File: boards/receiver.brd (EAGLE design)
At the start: 30 x 54.9 mm, 81 parts, among them IC2 7805DT, Q1 BC846BSMD, Q2 BC846BSMD, Q3 BC846BSMD, Q4 BC846BSMD, Q5 BC846BSMD, Q6 BC846BSMD, Q7 BC846BSMD, Q8 BC846BSMD

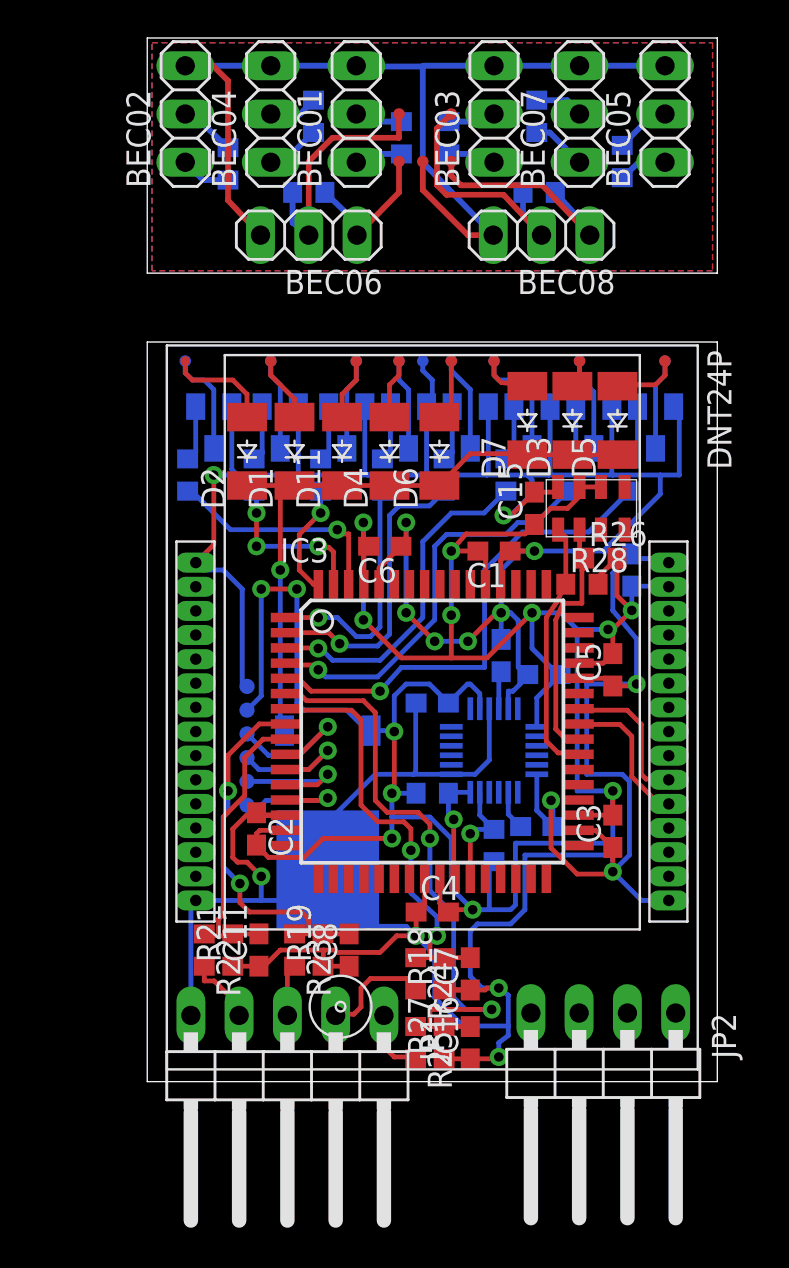
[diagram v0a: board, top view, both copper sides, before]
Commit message: Layout changes, all connections are routed now
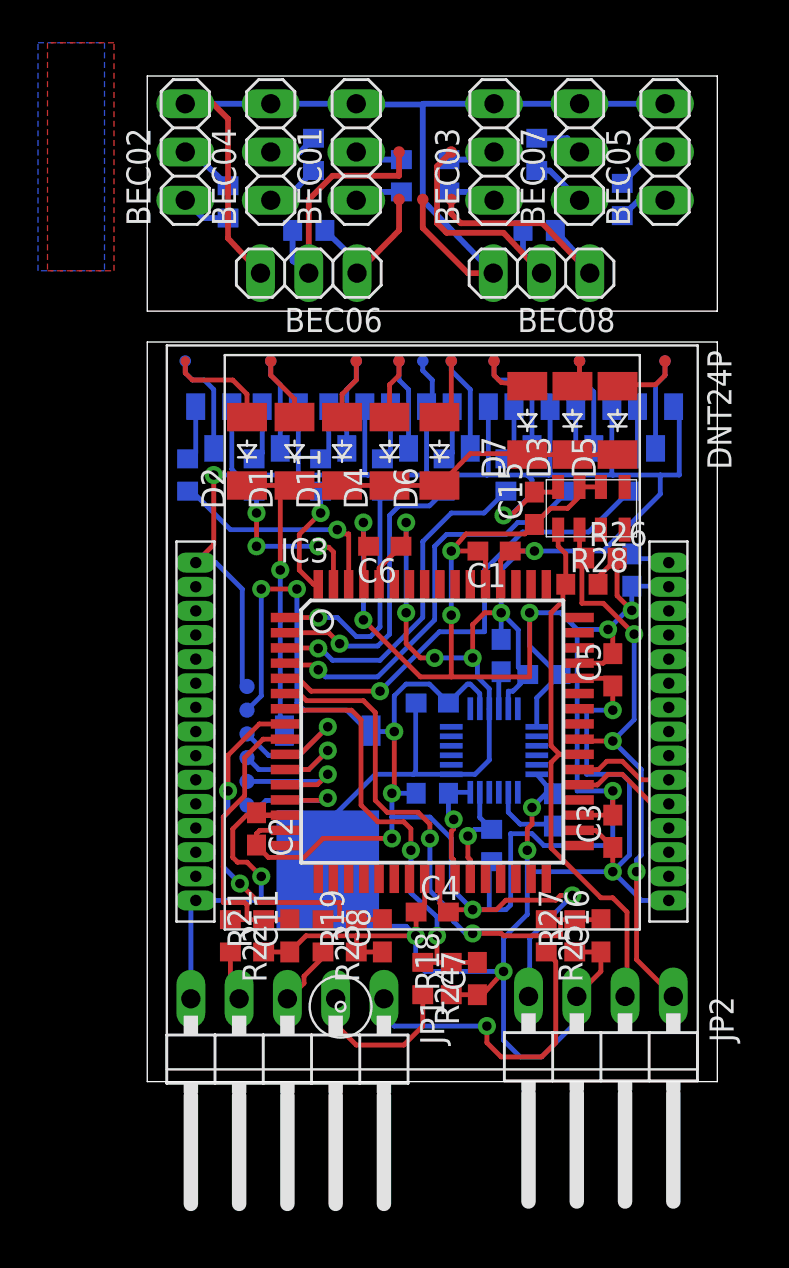
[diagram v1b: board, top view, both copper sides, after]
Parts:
- moved C16 8.88 mm to (24.9, 8.75)
- moved R25 8.88 mm to (22.0, 8.75)
- moved R27 8.88 mm to (23.5, 8.75)
- moved BEC01 2.00 mm to (12.0, 50.0)
- moved BEC02 2.00 mm to (3.00, 50.0)
- moved BEC03 2.00 mm to (19.2, 50.0)
- moved BEC04 2.00 mm to (7.50, 50.0)
- moved BEC05 2.00 mm to (28.2, 50.0)
- moved BEC06 2.00 mm to (9.50, 43.6)
- moved BEC07 2.00 mm to (23.8, 50.0)
- moved BEC08 2.00 mm to (21.8, 43.6)
- moved R10 2.00 mm to (26.0, 47.5)
- moved R12 2.00 mm to (9.50, 45.9)
- moved R14 2.00 mm to (21.5, 49.9)
- moved R16 2.00 mm to (21.6, 45.9)
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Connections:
- net +3V3: now also JP2.4
- net GND: now also JP2.3
- net N$33: now also IC3.37; no longer IC3.41
- net N$36: now also IC3.38; no longer IC3.42
- net N$46: now also JP2.2
- net N$47: now also JP2.1
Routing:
- net N$47: track 13.7 -> 30.7 mm, vias 0 -> 3
- net +3V3: track 149.3 -> 165.5 mm, vias 14 -> 15
- net N$46: track 13.6 -> 29.3 mm
- net GND: track 323.0 -> 308.9 mm
- net N$50: track 3.58 -> 16.6 mm, vias 0 -> 1
- net PB0: track 32.1 -> 28.5 mm
- net N$36: track 7.77 -> 5.28 mm
- net N$33: track 7.68 -> 5.58 mm
- net N$35: track 2.23 -> 4.24 mm
- net N$42: track 6.55 -> 8.45 mm
- net PB3: track 15.4 -> 16.9 mm
- net N$27: track 25.8 -> 24.7 mm
- net PB2: track 19.5 -> 20.6 mm
- net N$44: track 3.66 -> 2.66 mm
- net N$43: track 2.75 -> 3.61 mm
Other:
- board size 30 x 54.9 mm -> 30 x 52.9 mm

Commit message: rerouted some wires
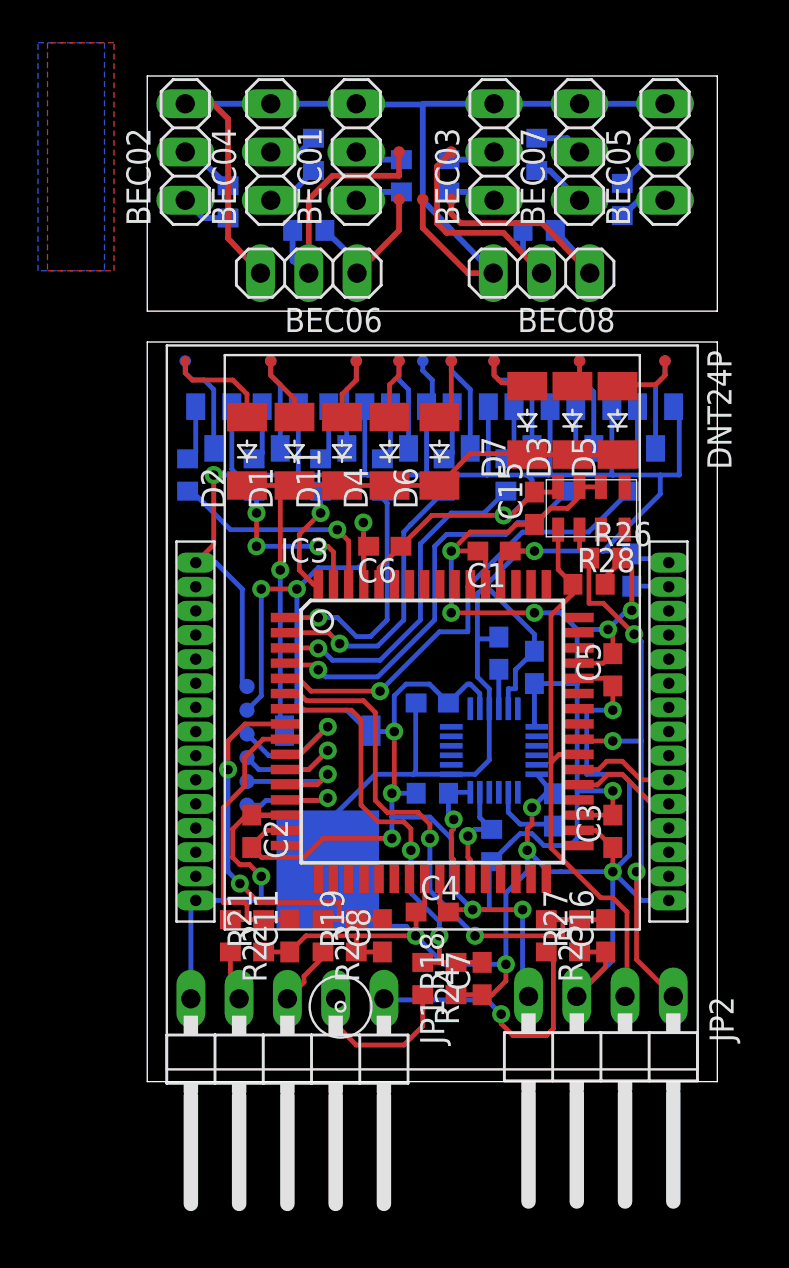
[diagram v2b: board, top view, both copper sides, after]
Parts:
- moved C14 0.62 mm to (21.4, 22.9), turned to 270 degrees
- moved R28 0.38 mm to (24.2, 27.2)
- moved C2 0.28 mm to (6.50, 14.2)
- moved C16 0.25 mm to (25.1, 8.75)
- moved C7 0.25 mm to (18.6, 6.50)
- moved R18 0.25 mm to (17.2, 6.50)
- moved R26 0.25 mm to (25.1, 28.6)
- moved R27 0.25 mm to (23.8, 8.75)
- moved C13 0.18 mm to (19.5, 23.6)
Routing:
- net +3V3: track 165.5 -> 141.5 mm, vias 15 -> 14
- net GND: track 308.9 -> 302.5 mm, vias 15 -> 10
- net N$50: track 16.6 -> 14.3 mm
- net N$31: track 15.7 -> 14.8 mm
- net N$46: track 29.3 -> 29.8 mm
- net N$27: track 24.7 -> 24.2 mm

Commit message: Added some passives for the voltage regulator.
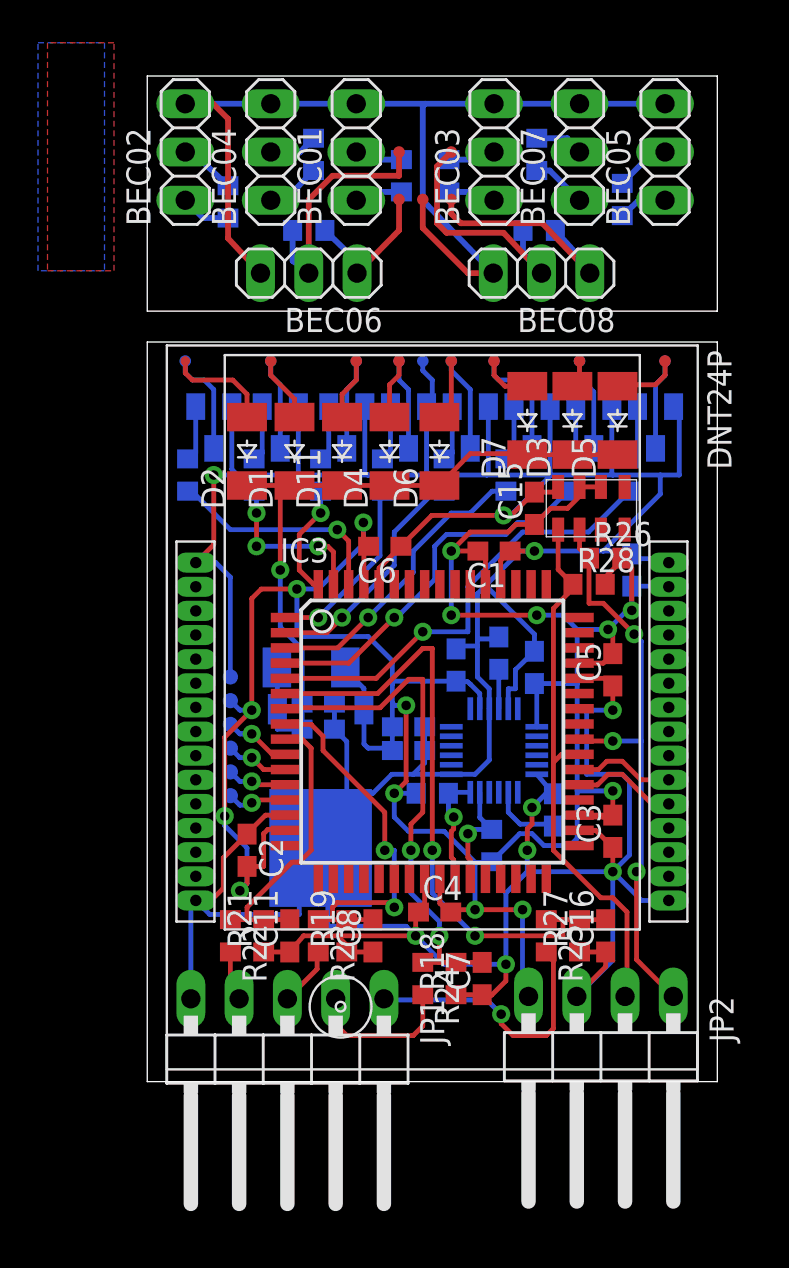
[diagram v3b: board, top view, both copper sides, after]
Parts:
- removed IC2: 7805DT, linear:TO252
- added C17, C19: 10µF, eagle-ltspice:C0603
- added C18, C21: 100nF, eagle-ltspice:C0603
- added D8: B 140 F, diode:SOD-123_MINI-SMA
- added IC1: 7805DT, linear:TO252
- C1, C11, C15, C16, C2, C3, C4, C5, C6, C7, C8, C9: value (none) -> 100nF
- C10: value (none) -> 2.2nF
- C12, C13: value (none) -> 0.1µF
- C14: value (none) -> 10nF
- IC3: value (none) -> XMEGA128a3u
- JP1: value (none) -> vSense
- JP2: value (none) -> i2c
- R1, R10, R11, R12, R13, R14, R15, R16, R17, R2, R20, R22, R23, R24, R25, R26, R28, R3, R4, R5, R6, R7, R8, R9: value (none) -> 10k
- R18, R19, R21, R27: value (none) -> 560
- moved C12 2.36 mm to (17.2, 23.0), turned to 270 degrees
- moved C2 1.03 mm to (6.25, 13.2)
- moved TP1 1.01 mm to (5.38, 17.4)
- moved TP2 1.01 mm to (5.38, 18.6)
- moved TP3 1.01 mm to (5.38, 19.9)
- moved TP4 1.01 mm to (5.38, 21.1)
- moved TP5 1.01 mm to (5.38, 22.4)
- moved TP7 1.01 mm to (5.38, 16.1)
- moved C8 0.50 mm to (12.9, 8.75)
- moved R19 0.50 mm to (11.5, 8.75)
- moved R23 0.25 mm to (10.0, 8.75)
- moved C4 0.12 mm to (16.1, 10.0)
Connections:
- removed net +3V3: C1.2, C12.2, C14.2, C15.1, C2.2, C3.2, C4.2, C5.2, C6.2, C9.2, IC2.2, IC3.15, IC3.25, IC3.35, IC3.45, IC3.53, IC3.61, JP2.4, R17.1, R20.1, R26.2, R28.2, TP4.TP, U$1.P14, U$2.P$2, U$2.P$3, U$3.P13, U$3.P8
- removed net N$34: D1.C, D11.C, D2.C, D3.C, D4.C, D5.C, D6.C, D7.C, IC2.1
- new net VCC: C1.2, C12.2, C14.2, C15.1, C18.2, C19.2, C2.2, C3.2, C4.2, C5.2, C6.2, C9.2, D8.A, IC1.2, IC3.15, IC3.25, IC3.35, IC3.45, IC3.53, IC3.61, JP2.4, R17.1, R20.1, R26.2, R28.2, TP4.TP, U$1.P14, U$2.P$2, U$2.P$3, U$3.P13, U$3.P8
- new net VDD: C17.2, C21.2, D1.C, D11.C, D2.C, D3.C, D4.C, D5.C, D6.C, D7.C, D8.C, IC1.1
- net GND: now also C17.1, C18.1, C19.1, C21.1, IC1.3; no longer IC2.3
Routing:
- net VCC: track 0.00 -> 152.7 mm, vias 0 -> 15
- net +3V3: track 141.5 -> 0.00 mm, vias 14 -> 0
- net VDD: track 0.00 -> 38.3 mm, vias 0 -> 1
- net N$34: track 33.4 -> 0.00 mm, vias 1 -> 0
- net PB0: track 28.6 -> 33.4 mm
- net N$38: track 8.19 -> 3.53 mm
- net GND: track 302.5 -> 306.7 mm, vias 10 -> 9
- net N$39: track 7.59 -> 3.34 mm
- net PB1: track 22.7 -> 26.8 mm
- net N$40: track 6.88 -> 3.15 mm
- net N$41: track 6.72 -> 3.17 mm
- net N$30: track 13.1 -> 9.78 mm
- net N$31: track 14.8 -> 12.5 mm
- net N$32: track 17.9 -> 15.7 mm
- net N$28: track 21.5 -> 19.6 mm
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
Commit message: Added some status leds
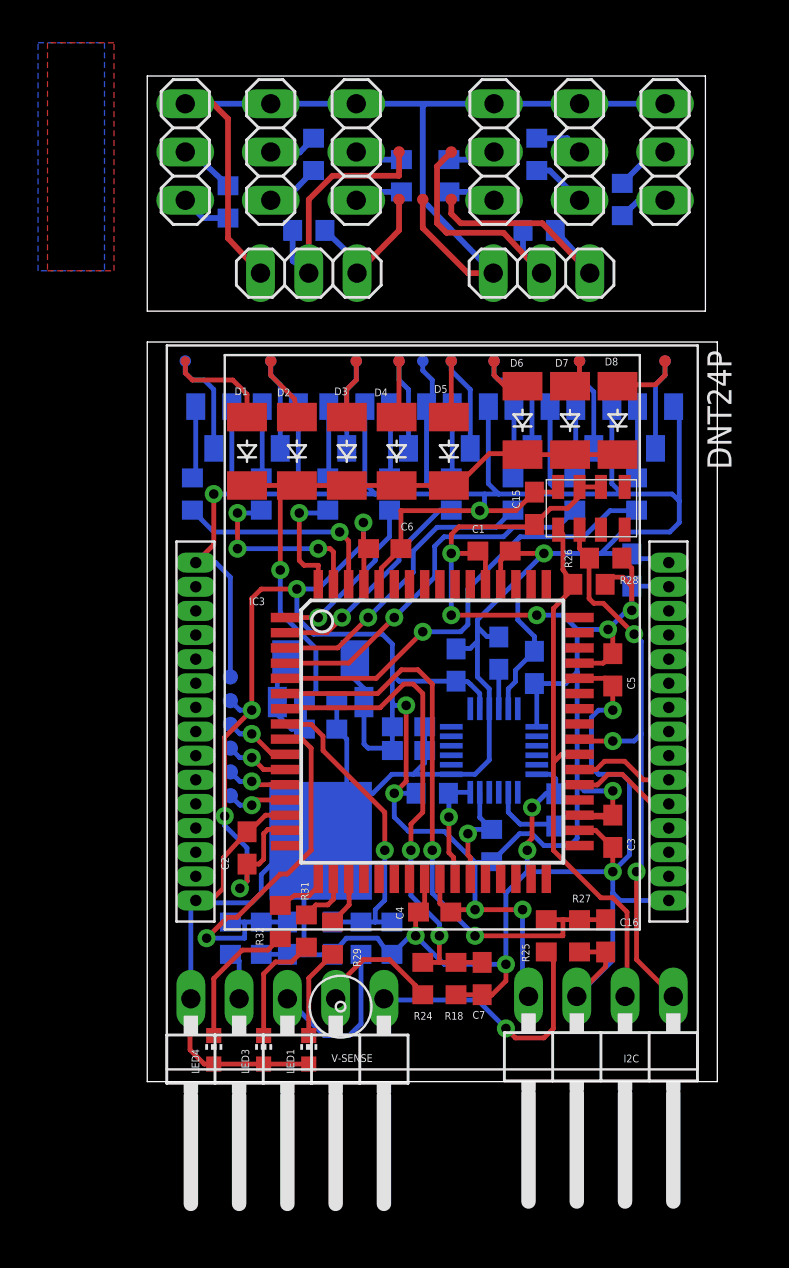
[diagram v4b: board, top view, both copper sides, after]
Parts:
- removed D11: B 140 F, diode:SOD-123_MINI-SMA
- added D9: B 140 F, diode:SOD-123_MINI-SMA
- added LED1: LS L29K, led:CHIP-LED0603
- added LED3: LO L29K, led:CHIP-LED0603
- added LED4: LG L29K, led:CHIP-LED0603
- added R29, R31, R32: 820, eagle-ltspice:R0603
- moved D8 20.7 mm to (25.8, 35.9), flipped to the top, turned to 90 degrees
- moved D3 12.0 mm to (11.5, 34.2)
- moved D5 9.02 mm to (16.9, 34.2)
- moved D6 4.67 mm to (20.8, 35.9)
- moved D2 2.62 mm to (8.88, 34.2)
- moved D1 2.50 mm to (6.25, 34.2)
- moved R19 2.38 mm to (13.9, 8.62), flipped to the bottom
- moved R23 2.25 mm to (12.2, 8.62), flipped to the bottom
- moved D7 2.25 mm to (23.2, 35.9)
- moved C8 2.13 mm to (10.8, 8.62), flipped to the bottom
- moved R1 1.07 mm to (7.00, 32.0)
- moved R11 1.07 mm to (13.8, 32.0)
- moved R13 1.07 mm to (23.5, 32.0)
- moved R15 1.07 mm to (17.0, 32.0)
- moved R3 1.07 mm to (10.5, 32.0)
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- renumbered BEC01 to SERVO3, BEC02 to SERVO1, BEC03 to SERVO4, BEC04 to SERVO2, BEC05 to SERVO6, BEC06 to SERVO7, BEC07 to SERVO5, BEC08 to SERVO8, JP1 to V-SENSE, JP2 to I2C, TP4 to 3.3V, TP5 to GND
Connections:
- new net N$34: LED1.C, R29.1
- new net N$45: IC3.17, R32.2
- new net N$48: IC3.18, R31.2
- new net N$49: LED3.C, R31.1
- new net N$51: LED4.C, R32.1
- new net N$52: IC3.19, R29.2
- net GND: now also LED1.A, LED3.A, LED4.A
- net N$12: now also D8.A; no longer D5.A
- net N$15: now also D2.A; no longer D1.A
- net N$20: now also D7.A; no longer D3.A
- net N$23: now also D5.A; no longer D6.A
- net N$3: now also D3.A; no longer D11.A
- net N$6: now also D1.A; no longer D2.A
- net N$9: now also D6.A; no longer D7.A
- net VCC: now also D9.A; no longer D8.A
- net VDD: now also D9.C; no longer D11.C
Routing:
- net GND: track 306.7 -> 317.4 mm
- net N$51: track 0.00 -> 7.39 mm
- net N$49: track 0.00 -> 6.08 mm
- net N$43: track 3.14 -> 8.59 mm
- net N$34: track 0.00 -> 4.79 mm
- net PB3: track 16.4 -> 20.2 mm, vias 0 -> 1
- net PB2: track 20.1 -> 16.7 mm, vias 2 -> 1
- net N$48: track 0.00 -> 2.85 mm
- net N$45: track 0.00 -> 2.76 mm
- net N$52: track 0.00 -> 2.64 mm
- net PB0: track 33.4 -> 31.4 mm
- net VDD: track 38.3 -> 40.0 mm
- net N$42: track 8.03 -> 6.59 mm
- net VCC: track 152.7 -> 154.1 mm
- net N$25: track 8.80 -> 9.97 mm
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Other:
- outline, holes or cut-outs redrawn

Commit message: Added another led, proper resistor values for voltage dividers, layout of silkscreen
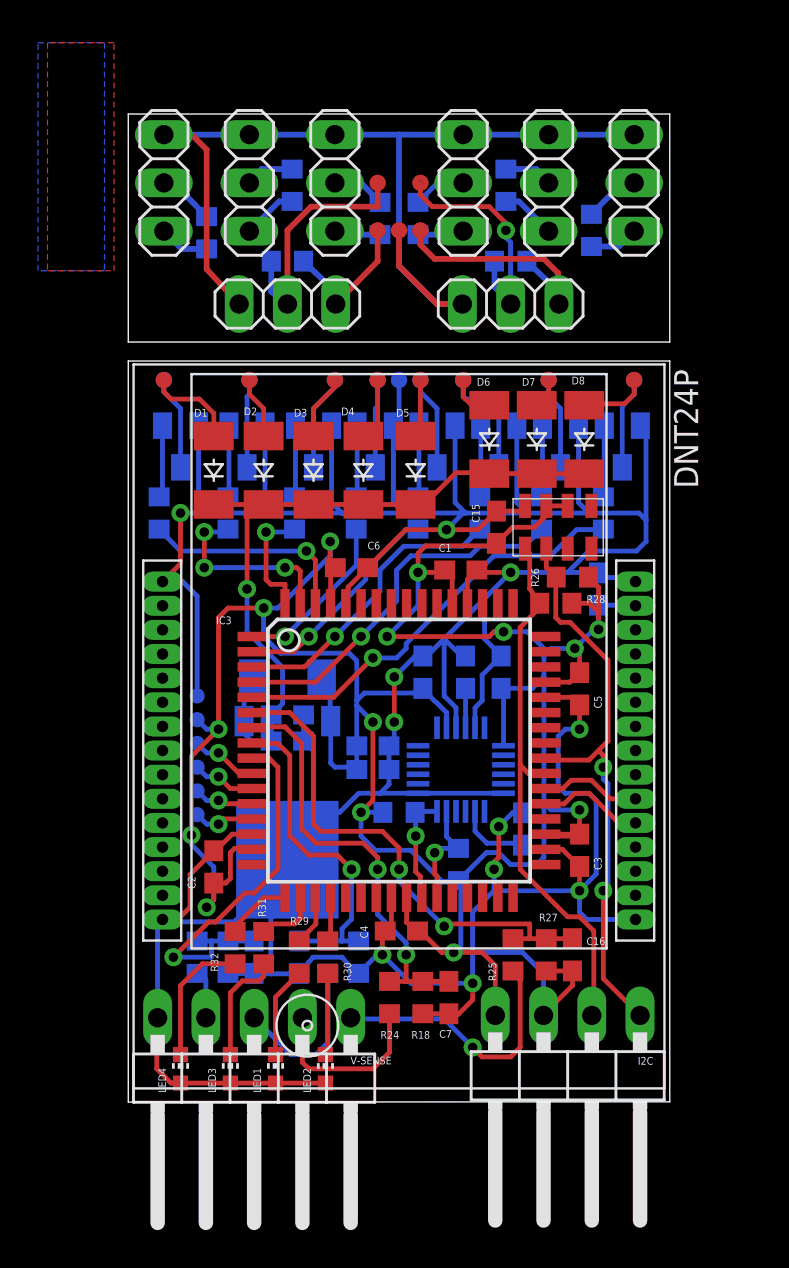
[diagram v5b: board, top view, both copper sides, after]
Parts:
- removed SERVO1, SERVO2, SERVO3, SERVO4, SERVO5, SERVO6, SERVO7, SERVO8: PCM, pinhead:1X03
- added LED2: LS L29K, led:CHIP-LED0603
- added R30: 820, eagle-ltspice:R0603
- added S1, S2, S3, S4, S5, S6, S7, S8: PCM, pinhead:1X03
- R22, R23, R24, R25: value 10k -> 2.2k
- moved R8 2.78 mm to (15.2, 46.5)
- moved R32 2.74 mm to (5.62, 8.12)
- moved R4 2.52 mm to (13.2, 46.5)
- moved R31 2.41 mm to (7.12, 8.12)
- moved R10 2.30 mm to (24.4, 45.9)
- moved R14 2.30 mm to (19.9, 48.2)
- moved C15 2.24 mm to (19.4, 30.2)
- moved R16 2.21 mm to (20.1, 44.2)
- moved C18 2.12 mm to (12.9, 18.8)
- moved C19 2.12 mm to (12.9, 17.5)
- moved 3.3V 2.02 mm to (3.62, 20.1)
- moved C1 2.02 mm to (17.5, 28.0)
- moved C10 2.02 mm to (20.8, 14.4)
- moved C11 2.02 mm to (6.62, 7.62)
- moved C13 2.02 mm to (17.8, 22.6)
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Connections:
- new net N$53: LED2.C, R30.1
- new net N$54: IC3.20, R30.2
- net GND: now also LED2.A, S1.3, S2.3, S3.3, S4.3, S5.3, S6.3, S7.3, S8.3; no longer SERVO1.3, SERVO2.3, SERVO3.3, SERVO4.3, SERVO5.3, SERVO6.3, SERVO7.3, SERVO8.3
- net N$11: now also S6.1; no longer SERVO6.1
- net N$12: now also S6.2; no longer SERVO6.2
- net N$14: now also S2.1; no longer SERVO2.1
- net N$15: now also S2.2; no longer SERVO2.2
- net N$16: now also S7.1; no longer SERVO7.1
- net N$17: now also S7.2; no longer SERVO7.2
- net N$19: now also S5.1; no longer SERVO5.1
- net N$2: now also S3.1; no longer SERVO3.1
- net N$20: now also S5.2; no longer SERVO5.2
- net N$22: now also S8.1; no longer SERVO8.1
- net N$23: now also S8.2; no longer SERVO8.2
- net N$3: now also S3.2; no longer SERVO3.2
- net N$5: now also S1.1; no longer SERVO1.1
- net N$6: now also S1.2; no longer SERVO1.2
- net N$8: now also S4.1; no longer SERVO4.1
- net N$9: now also S4.2; no longer SERVO4.2
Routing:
- net GND: track 317.4 -> 324.0 mm, vias 9 -> 11
- net VCC: track 154.1 -> 159.3 mm, vias 15 -> 14
- net N$53: track 0.00 -> 4.45 mm
- net PB0: track 31.4 -> 27.0 mm
- net PB1: track 26.1 -> 22.4 mm
- net N$42: track 6.59 -> 9.46 mm
- net N$54: track 0.00 -> 2.43 mm
- net N$27: track 23.3 -> 22.3 mm
- net PB2: track 16.7 -> 17.6 mm
- net N$22: track 17.3 -> 18.2 mm
- net N$45: track 2.76 -> 3.52 mm
- net N$5: track 8.22 -> 7.60 mm
- net N$23: track 16.3 -> 15.7 mm, vias 0 -> 1
- net N$6: track 8.49 -> 7.90 mm
- net VDD: track 40.0 -> 39.5 mm
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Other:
- board size 30 x 52.9 mm -> 28.5 x 52 mm
- board text added: "+"
- board text added: "-"
